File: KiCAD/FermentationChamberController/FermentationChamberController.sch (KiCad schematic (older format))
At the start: 18 parts, among them P1 Digital, P2 Analog

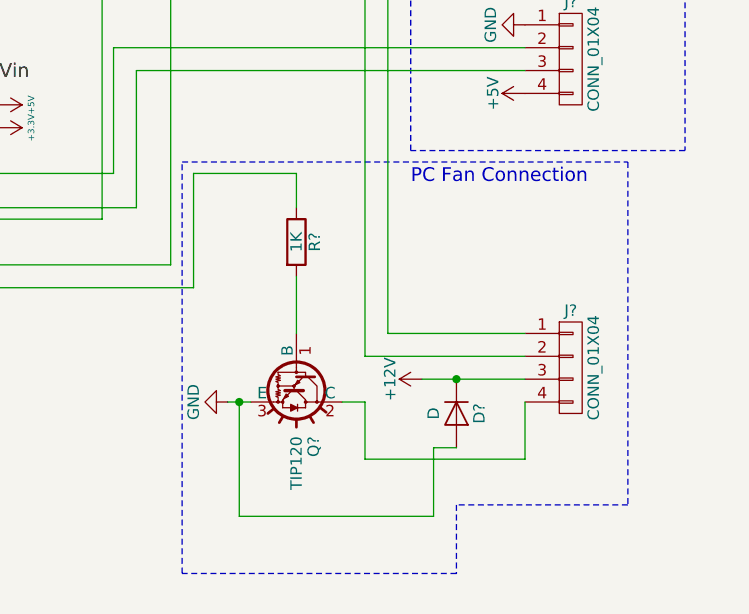
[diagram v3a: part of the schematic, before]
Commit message: And another correction to the diode
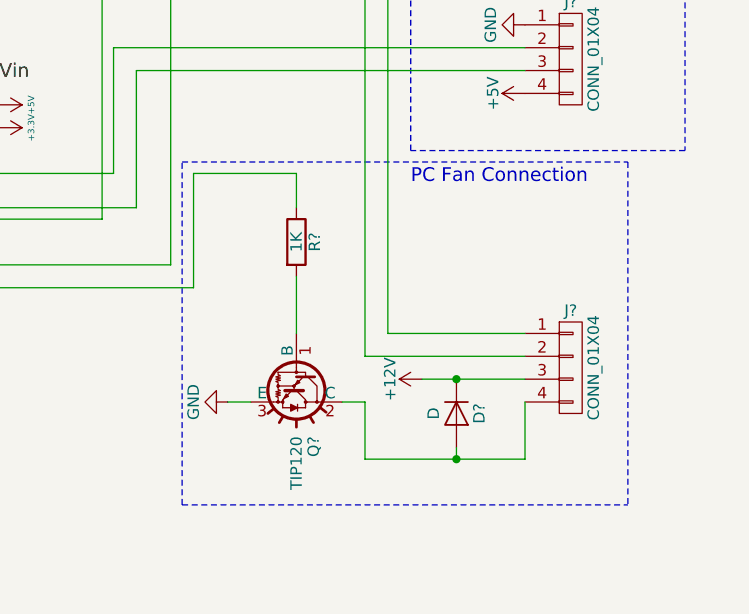
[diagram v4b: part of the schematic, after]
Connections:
- net GND: no longer D?.2 (A)
- net at J?.4 (P4), Q?.2 (C): now also D?.2 (A)
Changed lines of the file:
@@
 Wire Wire Line
 	5700 4900 5700 5050
-Connection ~ 5450 5900
 Wire Wire Line
 	5700 4900 5250 4900
@@
 	7400 3900 7400 4800
 Wire Notes Line
-	7150 6350 6400 6350
-Wire Notes Line
-	6400 6350 6400 6650
-Wire Notes Line
-	6400 6650 5200 6650
-Wire Notes Line
-	5200 6650 5200 4850
+	5200 6350 7150 6350
 Wire Notes Line
 	5200 4850 7150 4850
@@
 Connection ~ 6400 5800
 Wire Wire Line
-	5450 5900 5450 6400
-Wire Wire Line
-	5450 6400 6300 6400
-Wire Wire Line
-	6300 6400 6300 6100
-Wire Wire Line
-	6300 6100 6400 6100
-Wire Wire Line
 	6700 5900 6700 6150
 Wire Wire Line
@@
 Wire Wire Line
 	6000 6150 6000 5900
+Wire Wire Line
+	6400 6100 6400 6150
+Connection ~ 6400 6150
+Wire Notes Line
+	5200 6350 5200 4850
 $EndSCHEMATC

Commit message: Annotated
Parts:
- D1: renamed from D?; value D -> Diode
- gave numbers to parts that had none: 15
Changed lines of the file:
@@
 $EndComp
 $Comp
-L GND #PWR01
+L GND #PWR4
 U 1 1 56D7422C
 P 2750 3500
-F 0 "#PWR01" H 2750 3250 50  0001 C CNN
+F 0 "#PWR4" H 2750 3250 50  0001 C CNN
 F 1 "GND" H 2750 3350 50  0000 C CNN
 F 2 "" H 2750 3500 50  0000 C CNN
@@
 $EndComp
 $Comp
-L GND #PWR02
+L GND #PWR5
 U 1 1 56D746ED
 P 2750 4500
-F 0 "#PWR02" H 2750 4250 50  0001 C CNN
+F 0 "#PWR5" H 2750 4250 50  0001 C CNN
 F 1 "GND" H 2750 4350 50  0000 C CNN
 F 2 "" H 2750 4500 50  0000 C CNN
@@
 $EndComp
 $Comp
-L +5V #PWR03
+L +5V #PWR11
 U 1 1 56D747E8
 P 4400 4600
-F 0 "#PWR03" H 4400 4450 50  0001 C CNN
+F 0 "#PWR11" H 4400 4450 50  0001 C CNN
 F 1 "+5V" H 4400 4740 28  0000 C CNN
 F 2 "" H 4400 4600 50  0000 C CNN
@@
 $EndComp
 $Comp
-L +3.3V #PWR04
+L +3.3V #PWR12
 U 1 1 56D74854
 P 4400 4700
-F 0 "#PWR04" H 4400 4550 50  0001 C CNN
+F 0 "#PWR12" H 4400 4550 50  0001 C CNN
 F 1 "+3.3V" H 4400 4840 28  0000 C CNN
 F 2 "" H 4400 4700 50  0000 C CNN
@@
 1
 $Comp
-L LCD16X2 DS?
+L LCD16X2 DS1
 U 1 1 591B37D5
 P 3500 1150
-F 0 "DS?" H 2700 1550 50  0000 C CNN
+F 0 "DS1" H 2700 1550 50  0000 C CNN
 F 1 "LCD16X2" H 4200 1550 50  0000 C CNN
 F 2 "WC1602A" H 3500 1100 50  0001 C CIN
@@
 $EndComp
 $Comp
-L TIP120 Q?
+L TIP120 Q1
 U 1 1 591B3DDF
 P 5200 2150
-F 0 "Q?" H 5450 2225 50  0000 L CNN
+F 0 "Q1" H 5450 2225 50  0000 L CNN
 F 1 "TIP120" H 5450 2150 50  0000 L CNN
 F 2 "TO_SOT_Packages_THT:TO-220_Vertical" H 5450 2075 50  0001 L CIN
@@
 $EndComp
 $Comp
-L R R?
+L R R2
 U 1 1 591B3E76
 P 2950 2100
-F 0 "R?" V 3030 2100 50  0000 C CNN
+F 0 "R2" V 3030 2100 50  0000 C CNN
 F 1 "1.47K" V 2950 2100 50  0000 C CNN
 F 2 "" V 2880 2100 50  0001 C CNN
@@
 $EndComp
 $Comp
-L R R?
+L R R3
 U 1 1 591B3EE1
 P 4150 1850
-F 0 "R?" V 4230 1850 50  0000 C CNN
+F 0 "R3" V 4230 1850 50  0000 C CNN
 F 1 "220" V 4150 1850 50  0000 C CNN
 F 2 "" V 4080 1850 50  0001 C CNN
@@
 $EndComp
 $Comp
-L R R?
+L R R4
 U 1 1 591B3F3C
 P 4850 2350
-F 0 "R?" V 4930 2350 50  0000 C CNN
+F 0 "R4" V 4930 2350 50  0000 C CNN
 F 1 "2K" V 4850 2350 50  0000 C CNN
 F 2 "" V 4780 2350 50  0001 C CNN
@@
 	5300 1650 5300 1950
 $Comp
-L Earth #PWR?
+L Earth #PWR13
 U 1 1 591B481E
 P 5300 2400
-F 0 "#PWR?" H 5300 2150 50  0001 C CNN
+F 0 "#PWR13" H 5300 2150 50  0001 C CNN
 F 1 "Earth" H 5300 2250 50  0001 C CNN
 F 2 "" H 5300 2400 50  0001 C CNN
@@
 	5300 2400 5300 2350
 $Comp
-L Earth #PWR?
+L Earth #PWR3
 U 1 1 591B4871
 P 2750 1700
-F 0 "#PWR?" H 2750 1450 50  0001 C CNN
+F 0 "#PWR3" H 2750 1450 50  0001 C CNN
 F 1 "Earth" H 2750 1550 50  0001 C CNN
 F 2 "" H 2750 1700 50  0001 C CNN
@@
 	2750 1650 2750 1700
 $Comp
-L +5V #PWR?
+L +5V #PWR7
 U 1 1 591B4919
 P 2850 1700
-F 0 "#PWR?" H 2850 1550 50  0001 C CNN
+F 0 "#PWR7" H 2850 1550 50  0001 C CNN
 F 1 "+5V" H 2850 1840 50  0000 C CNN
 F 2 "" H 2850 1700 50  0001 C CNN
@@
 	2950 1650 2950 1950
 $Comp
-L Earth #PWR?
+L Earth #PWR8
 U 1 1 591B4B94
 P 2950 2250
-F 0 "#PWR?" H 2950 2000 50  0001 C CNN
+F 0 "#PWR8" H 2950 2000 50  0001 C CNN
 F 1 "Earth" H 2950 2100 50  0001 C CNN
 F 2 "" H 2950 2250 50  0001 C CNN
@@
 	4850 5100 2850 5100
 $Comp
-L Earth #PWR?
+L Earth #PWR9
 U 1 1 591B5084
 P 3150 1700
-F 0 "#PWR?" H 3150 1450 50  0001 C CNN
+F 0 "#PWR9" H 3150 1450 50  0001 C CNN
 F 1 "Earth" H 3150 1550 50  0001 C CNN
 F 2 "" H 3150 1700 50  0001 C CNN
@@
 	4150 1650 4150 1700
 $Comp
-L +5V #PWR?
+L +5V #PWR10
 U 1 1 591BA361
 P 4150 2000
-F 0 "#PWR?" H 4150 1850 50  0001 C CNN
+F 0 "#PWR10" H 4150 1850 50  0001 C CNN
 F 1 "+5V" H 4150 2140 50  0000 C CNN
 F 2 "" H 4150 2000 50  0001 C CNN
@@
 $EndComp
 $Comp
-L Rotary_Encoder_Switch SW?
+L Rotary_Encoder_Switch SW1
 U 1 1 591BA40F
 P 6100 1200
-F 0 "SW?" H 6100 1460 50  0000 C CNN
+F 0 "SW1" H 6100 1460 50  0000 C CNN
 F 1 "Rotary_Encoder_Switch" H 6100 940 50  0000 C CNN
 F 2 "" H 6000 1360 50  0001 C CNN
@@
 	6650 1300 6400 1300
 $Comp
-L +5V #PWR?
+L +5V #PWR17
 U 1 1 591BA55B
 P 6450 1100
-F 0 "#PWR?" H 6450 950 50  0001 C CNN
+F 0 "#PWR17" H 6450 950 50  0001 C CNN
 F 1 "+5V" H 6450 1240 50  0000 C CNN
 F 2 "" H 6450 1100 50  0001 C CNN
@@
 	6400 1100 6450 1100
 $Comp
-L R R?
+L R R6
 U 1 1 591BA5F0
 P 6800 1300
-F 0 "R?" V 6880 1300 50  0000 C CNN
+F 0 "R6" V 6880 1300 50  0000 C CNN
 F 1 "10K" V 6800 1300 50  0000 C CNN
 F 2 "" V 6730 1300 50  0001 C CNN
@@
 $EndComp
 $Comp
-L GND #PWR?
+L GND #PWR20
 U 1 1 591BA655
 P 7000 1300
-F 0 "#PWR?" H 7000 1050 50  0001 C CNN
+F 0 "#PWR20" H 7000 1050 50  0001 C CNN
 F 1 "GND" H 7000 1150 50  0000 C CNN
 F 2 "" H 7000 1300 50  0001 C CNN
@@
 	7000 1300 6950 1300
 $Comp
-L GND #PWR?
+L GND #PWR15
 U 1 1 591BA8F3
 P 5750 1200
-F 0 "#PWR?" H 5750 950 50  0001 C CNN
+F 0 "#PWR15" H 5750 950 50  0001 C CNN
 F 1 "GND" H 5750 1050 50  0000 C CNN
 F 2 "" H 5750 1200 50  0001 C CNN
@@
 	4650 1100 5800 1100
 $Comp
-L Screw_Terminal_1x02 J?
+L Screw_Terminal_1x02 J1
 U 1 1 591BAA85
 P 1000 6500
-F 0 "J?" H 1000 6750 50  0000 C TNN
+F 0 "J1" H 1000 6750 50  0000 C TNN
 F 1 "Screw_Terminal_1x02" V 850 6500 50  0000 C TNN
 F 2 "" H 1000 6275 50  0001 C CNN
@@
 $EndComp
 $Comp
-L Screw_Terminal_1x02 J?
+L Screw_Terminal_1x02 J2
 U 1 1 591BADC2
 P 1850 6500
-F 0 "J?" H 1850 6750 50  0000 C TNN
+F 0 "J2" H 1850 6750 50  0000 C TNN
 F 1 "Screw_Terminal_1x02" V 1700 6500 50  0000 C TNN
 F 2 "" H 1850 6275 50  0001 C CNN
@@
 $EndComp
 $Comp
-L Screw_Terminal_1x02 J?
+L Screw_Terminal_1x02 J3
 U 1 1 591BAE99
 P 2700 6500
-F 0 "J?" H 2700 6750 50  0000 C TNN
+F 0 "J3" H 2700 6750 50  0000 C TNN
 F 1 "Screw_Terminal_1x02" V 2550 6500 50  0000 C TNN
 F 2 "" H 2700 6275 50  0001 C CNN
@@
 Connection ~ 1750 5800
 $Comp
-L R R?
+L R R1
 U 1 1 591BB000
 P 1900 5550
-F 0 "R?" V 1980 5550 50  0000 C CNN
+F 0 "R1" V 1980 5550 50  0000 C CNN
 F 1 "4.7K" V 1800 5550 50  0000 C CNN
 F 2 "" V 1830 5550 50  0001 C CNN
@@
 $EndComp
 $Comp
-L +5V #PWR?
+L +5V #PWR2
 U 1 1 591BB0B3
 P 2150 5550
-F 0 "#PWR?" H 2150 5400 50  0001 C CNN
+F 0 "#PWR2" H 2150 5400 50  0001 C CNN
 F 1 "+5V" H 2150 5690 50  0000 C CNN
 F 2 "" H 2150 5550 50  0001 C CNN
@@
 Connection ~ 2150 5700
 $Comp
-L GND #PWR?
+L GND #PWR1
 U 1 1 591BB21C
 P 900 6200
-F 0 "#PWR?" H 900 5950 50  0001 C CNN
+F 0 "#PWR1" H 900 5950 50  0001 C CNN
 F 1 "GND" H 900 6050 50  0000 C CNN
 F 2 "" H 900 6200 50  0001 C CNN
@@
 $EndComp
 $Comp
-L GND #PWR?
+L GND #PWR6
 U 1 1 591BB255
 P 2800 6200
-F 0 "#PWR?" H 2800 5950 50  0001 C CNN
+F 0 "#PWR6" H 2800 5950 50  0001 C CNN
 F 1 "GND" H 2800 6050 50  0000 C CNN
 F 2 "" H 2800 6200 50  0001 C CNN
@@
 	3150 2800 3150 3600
 $Comp
-L CONN_01X04 J?
+L CONN_01X04 J5
 U 1 1 591BC121
 P 6900 5750
-F 0 "J?" H 6900 6000 50  0000 C CNN
+F 0 "J5" H 6900 6000 50  0000 C CNN
 F 1 "CONN_01X04" V 7000 5750 50  0000 C CNN
 F 2 "" H 6900 5750 50  0001 C CNN
@@
 $EndComp
 $Comp
-L TIP120 Q?
+L TIP120 Q2
 U 1 1 591BC33E
 P 5700 5800
-F 0 "Q?" H 5950 5875 50  0000 L CNN
+F 0 "Q2" H 5950 5875 50  0000 L CNN
 F 1 "TIP120" H 5950 5800 50  0000 L CNN
 F 2 "TO_SOT_Packages_THT:TO-220_Vertical" H 5950 5725 50  0001 L CIN
@@
 $EndComp
 $Comp
-L CONN_01X04 J?
+L CONN_01X04 J4
 U 1 1 591BC4F4
 P 6900 4400
-F 0 "J?" H 6900 4650 50  0000 C CNN
+F 0 "J4" H 6900 4650 50  0000 C CNN
 F 1 "CONN_01X04" V 7000 4400 50  0000 C CNN
 F 2 "" H 6900 4400 50  0001 C CNN
@@
 $EndComp
 $Comp
-L D D?
+L D D1
 U 1 1 591BC636
 P 6400 5950
-F 0 "D?" H 6400 6050 50  0000 C CNN
-F 1 "D" H 6400 5850 50  0000 C CNN
+F 0 "D1" H 6400 6050 50  0000 C CNN
+F 1 "Diode" H 6400 5850 50  0000 C CNN
 F 2 "" H 6400 5950 50  0001 C CNN
 F 3 "" H 6400 5950 50  0001 C CNN
@@
 $EndComp
 $Comp
-L R R?
+L R R5
 U 1 1 591BC750
 P 5700 5200
-F 0 "R?" V 5780 5200 50  0000 C CNN
+F 0 "R5" V 5780 5200 50  0000 C CNN
 F 1 "1K" V 5700 5200 50  0000 C CNN
 F 2 "" V 5630 5200 50  0001 C CNN
@@
 $EndComp
 $Comp
-L GND #PWR?
+L GND #PWR14
 U 1 1 591BCA6D
 P 5400 5900
-F 0 "#PWR?" H 5400 5650 50  0001 C CNN
+F 0 "#PWR14" H 5400 5650 50  0001 C CNN
 F 1 "GND" H 5400 5750 50  0000 C CNN
 F 2 "" H 5400 5900 50  0001 C CNN
@@
 	6100 2800 3850 2800
 $Comp
-L +5V #PWR?
+L +5V #PWR19
 U 1 1 591BDC18
 P 6700 4550
-F 0 "#PWR?" H 6700 4400 50  0001 C CNN
+F 0 "#PWR19" H 6700 4400 50  0001 C CNN
 F 1 "+5V" H 6700 4690 50  0000 C CNN
 F 2 "" H 6700 4550 50  0001 C CNN
@@
 	4900 4900 3350 4900
 $Comp
-L GND #PWR?
+L GND #PWR18
 U 1 1 591BE258
 P 6700 4250
-F 0 "#PWR?" H 6700 4000 50  0001 C CNN
+F 0 "#PWR18" H 6700 4000 50  0001 C CNN
 F 1 "GND" H 6700 4100 50  0000 C CNN
 F 2 "" H 6700 4250 50  0001 C CNN
@@
 Arduino Nano
 $Comp
-L +12V #PWR?
+L +12V #PWR16
 U 1 1 591BFE81
 P 6250 5800
-F 0 "#PWR?" H 6250 5650 50  0001 C CNN
+F 0 "#PWR16" H 6250 5650 50  0001 C CNN
 F 1 "+12V" H 6250 5940 50  0000 C CNN
 F 2 "" H 6250 5800 50  0001 C CNN

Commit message: Workign on the PCB Layout, first step.
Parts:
- D1: footprint (none) -> Diodes_THT:D_DO-15_P10.16mm_Horizontal
- DS1: footprint WC1602A -> Pin_Headers:Pin_Header_Straight_1x16_Pitch2.54mm
- J1, J2, J3: footprint (none) -> Connectors_Terminal_Blocks:TerminalBlock_WAGO-804_RM5mm_2pol
- J4, J5: footprint (none) -> Pin_Headers:Pin_Header_Straight_1x04_Pitch2.54mm
- P1, P2: footprint Socket_Arduino_Nano:Socket_Strip_Arduino_1x15 -> Pin_Headers:Pin_Header_Straight_1x15_Pitch2.54mm
- Q1: footprint TO_SOT_Packages_THT:TO-220_Vertical -> TO_SOT_Packages_THT:TO-220_Horizontal
- R1, R2, R3, R4, R5, R6: footprint (none) -> Resistors_THT:R_Axial_DIN0207_L6.3mm_D2.5mm_P10.16mm_Horizontal
- SW1: footprint (none) -> Pin_Headers:Pin_Header_Straight_1x05_Pitch2.54mm
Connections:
- net 10(**/SS): now also R1.1
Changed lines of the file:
@@
 F 0 "P1" H 3550 4600 50  0000 C CNN
 F 1 "Digital" V 3650 3800 50  0000 C CNN
-F 2 "Socket_Arduino_Nano:Socket_Strip_Arduino_1x15" H 3550 3800 50  0001 C CNN
+F 2 "Pin_Headers:Pin_Header_Straight_1x15_Pitch2.54mm" H 3550 3800 50  0001 C CNN
 F 3 "" H 3550 3800 50  0000 C CNN
 	1    3550 3800
@@
 F 0 "P2" H 3550 5000 50  0000 C CNN
 F 1 "Analog" V 3650 4200 50  0000 C CNN
-F 2 "Socket_Arduino_Nano:Socket_Strip_Arduino_1x15" H 3550 4200 50  0001 C CNN
+F 2 "Pin_Headers:Pin_Header_Straight_1x15_Pitch2.54mm" H 3550 4200 50  0001 C CNN
 F 3 "" H 3550 4200 50  0000 C CNN
 	1    3550 4200
@@
 $EndComp
 $Comp
-L GND #PWR4
+L GND #PWR01
 U 1 1 56D7422C
 P 2750 3500
-F 0 "#PWR4" H 2750 3250 50  0001 C CNN
+F 0 "#PWR01" H 2750 3250 50  0001 C CNN
 F 1 "GND" H 2750 3350 50  0000 C CNN
 F 2 "" H 2750 3500 50  0000 C CNN
@@
 $EndComp
 $Comp
-L GND #PWR5
+L GND #PWR02
 U 1 1 56D746ED
 P 2750 4500
-F 0 "#PWR5" H 2750 4250 50  0001 C CNN
+F 0 "#PWR02" H 2750 4250 50  0001 C CNN
 F 1 "GND" H 2750 4350 50  0000 C CNN
 F 2 "" H 2750 4500 50  0000 C CNN
@@
 $EndComp
 $Comp
-L +5V #PWR11
+L +5V #PWR03
 U 1 1 56D747E8
 P 4400 4600
-F 0 "#PWR11" H 4400 4450 50  0001 C CNN
+F 0 "#PWR03" H 4400 4450 50  0001 C CNN
 F 1 "+5V" H 4400 4740 28  0000 C CNN
 F 2 "" H 4400 4600 50  0000 C CNN
@@
 $EndComp
 $Comp
-L +3.3V #PWR12
+L +3.3V #PWR04
 U 1 1 56D74854
 P 4400 4700
-F 0 "#PWR12" H 4400 4550 50  0001 C CNN
+F 0 "#PWR04" H 4400 4550 50  0001 C CNN
 F 1 "+3.3V" H 4400 4840 28  0000 C CNN
 F 2 "" H 4400 4700 50  0000 C CNN
@@
 F 0 "DS1" H 2700 1550 50  0000 C CNN
 F 1 "LCD16X2" H 4200 1550 50  0000 C CNN
-F 2 "WC1602A" H 3500 1100 50  0001 C CIN
+F 2 "Pin_Headers:Pin_Header_Straight_1x16_Pitch2.54mm" H 3500 1100 50  0001 C CIN
 F 3 "" H 3500 1150 50  0001 C CNN
 	1    3500 1150
@@
 F 0 "Q1" H 5450 2225 50  0000 L CNN
 F 1 "TIP120" H 5450 2150 50  0000 L CNN
-F 2 "TO_SOT_Packages_THT:TO-220_Vertical" H 5450 2075 50  0001 L CIN
+F 2 "TO_SOT_Packages_THT:TO-220_Horizontal" H 5450 2075 50  0001 L CIN
 F 3 "" H 5200 2150 50  0001 L CNN
 	1    5200 2150
@@
 F 0 "R2" V 3030 2100 50  0000 C CNN
 F 1 "1.47K" V 2950 2100 50  0000 C CNN
-F 2 "" V 2880 2100 50  0001 C CNN
+F 2 "Resistors_THT:R_Axial_DIN0207_L6.3mm_D2.5mm_P10.16mm_Horizontal" V 2880 2100 50  0001 C CNN
 F 3 "" H 2950 2100 50  0001 C CNN
 	1    2950 2100
@@
 F 0 "R3" V 4230 1850 50  0000 C CNN
 F 1 "220" V 4150 1850 50  0000 C CNN
-F 2 "" V 4080 1850 50  0001 C CNN
+F 2 "Resistors_THT:R_Axial_DIN0207_L6.3mm_D2.5mm_P10.16mm_Horizontal" V 4080 1850 50  0001 C CNN
 F 3 "" H 4150 1850 50  0001 C CNN
 	1    4150 1850
@@
 F 0 "R4" V 4930 2350 50  0000 C CNN
 F 1 "2K" V 4850 2350 50  0000 C CNN
-F 2 "" V 4780 2350 50  0001 C CNN
+F 2 "Resistors_THT:R_Axial_DIN0207_L6.3mm_D2.5mm_P10.16mm_Horizontal" V 4780 2350 50  0001 C CNN
 F 3 "" H 4850 2350 50  0001 C CNN
 	1    4850 2350
@@
 	5300 1650 5300 1950
 $Comp
-L Earth #PWR13
+L Earth #PWR05
 U 1 1 591B481E
 P 5300 2400
-F 0 "#PWR13" H 5300 2150 50  0001 C CNN
+F 0 "#PWR05" H 5300 2150 50  0001 C CNN
 F 1 "Earth" H 5300 2250 50  0001 C CNN
 F 2 "" H 5300 2400 50  0001 C CNN
@@
 	5300 2400 5300 2350
 $Comp
-L Earth #PWR3
+L Earth #PWR06
 U 1 1 591B4871
 P 2750 1700
-F 0 "#PWR3" H 2750 1450 50  0001 C CNN
+F 0 "#PWR06" H 2750 1450 50  0001 C CNN
 F 1 "Earth" H 2750 1550 50  0001 C CNN
 F 2 "" H 2750 1700 50  0001 C CNN
@@
 	2750 1650 2750 1700
 $Comp
-L +5V #PWR7
+L +5V #PWR07
 U 1 1 591B4919
 P 2850 1700
-F 0 "#PWR7" H 2850 1550 50  0001 C CNN
+F 0 "#PWR07" H 2850 1550 50  0001 C CNN
 F 1 "+5V" H 2850 1840 50  0000 C CNN
 F 2 "" H 2850 1700 50  0001 C CNN
@@
 	2950 1650 2950 1950
 $Comp
-L Earth #PWR8
+L Earth #PWR08
 U 1 1 591B4B94
 P 2950 2250
-F 0 "#PWR8" H 2950 2000 50  0001 C CNN
+F 0 "#PWR08" H 2950 2000 50  0001 C CNN
 F 1 "Earth" H 2950 2100 50  0001 C CNN
 F 2 "" H 2950 2250 50  0001 C CNN
@@
 	4850 5100 2850 5100
 $Comp
-L Earth #PWR9
+L Earth #PWR09
 U 1 1 591B5084
 P 3150 1700
-F 0 "#PWR9" H 3150 1450 50  0001 C CNN
+F 0 "#PWR09" H 3150 1450 50  0001 C CNN
 F 1 "Earth" H 3150 1550 50  0001 C CNN
 F 2 "" H 3150 1700 50  0001 C CNN
@@
 	4150 1650 4150 1700
 $Comp
-L +5V #PWR10
+L +5V #PWR010
 U 1 1 591BA361
 P 4150 2000
-F 0 "#PWR10" H 4150 1850 50  0001 C CNN
+F 0 "#PWR010" H 4150 1850 50  0001 C CNN
 F 1 "+5V" H 4150 2140 50  0000 C CNN
 F 2 "" H 4150 2000 50  0001 C CNN
@@
 F 0 "SW1" H 6100 1460 50  0000 C CNN
 F 1 "Rotary_Encoder_Switch" H 6100 940 50  0000 C CNN
-F 2 "" H 6000 1360 50  0001 C CNN
+F 2 "Pin_Headers:Pin_Header_Straight_1x05_Pitch2.54mm" H 6000 1360 50  0001 C CNN
 F 3 "" H 6100 1460 50  0001 C CNN
 	1    6100 1200
@@
 	6650 1300 6400 1300
 $Comp
-L +5V #PWR17
+L +5V #PWR011
 U 1 1 591BA55B
 P 6450 1100
-F 0 "#PWR17" H 6450 950 50  0001 C CNN
+F 0 "#PWR011" H 6450 950 50  0001 C CNN
 F 1 "+5V" H 6450 1240 50  0000 C CNN
 F 2 "" H 6450 1100 50  0001 C CNN
@@
 F 0 "R6" V 6880 1300 50  0000 C CNN
 F 1 "10K" V 6800 1300 50  0000 C CNN
-F 2 "" V 6730 1300 50  0001 C CNN
+F 2 "Resistors_THT:R_Axial_DIN0207_L6.3mm_D2.5mm_P10.16mm_Horizontal" V 6730 1300 50  0001 C CNN
 F 3 "" H 6800 1300 50  0001 C CNN
 	1    6800 1300
@@
 $EndComp
 $Comp
-L GND #PWR20
+L GND #PWR012
 U 1 1 591BA655
 P 7000 1300
-F 0 "#PWR20" H 7000 1050 50  0001 C CNN
+F 0 "#PWR012" H 7000 1050 50  0001 C CNN
 F 1 "GND" H 7000 1150 50  0000 C CNN
 F 2 "" H 7000 1300 50  0001 C CNN
@@
 	7000 1300 6950 1300
 $Comp
-L GND #PWR15
+L GND #PWR013
 U 1 1 591BA8F3
 P 5750 1200
-F 0 "#PWR15" H 5750 950 50  0001 C CNN
+F 0 "#PWR013" H 5750 950 50  0001 C CNN
 F 1 "GND" H 5750 1050 50  0000 C CNN
 F 2 "" H 5750 1200 50  0001 C CNN
@@
 F 0 "J1" H 1000 6750 50  0000 C TNN
 F 1 "Screw_Terminal_1x02" V 850 6500 50  0000 C TNN
-F 2 "" H 1000 6275 50  0001 C CNN
+F 2 "Connectors_Terminal_Blocks:TerminalBlock_WAGO-804_RM5mm_2pol" H 1000 6275 50  0001 C CNN
 F 3 "" H 975 6500 50  0001 C CNN
 	1    1000 6500
@@
 F 0 "J2" H 1850 6750 50  0000 C TNN
 F 1 "Screw_Terminal_1x02" V 1700 6500 50  0000 C TNN
-F 2 "" H 1850 6275 50  0001 C CNN
+F 2 "Connectors_Terminal_Blocks:TerminalBlock_WAGO-804_RM5mm_2pol" H 1850 6275 50  0001 C CNN
 F 3 "" H 1825 6500 50  0001 C CNN
 	1    1850 6500
@@
 F 0 "J3" H 2700 6750 50  0000 C TNN
 F 1 "Screw_Terminal_1x02" V 2550 6500 50  0000 C TNN
-F 2 "" H 2700 6275 50  0001 C CNN
+F 2 "Connectors_Terminal_Blocks:TerminalBlock_WAGO-804_RM5mm_2pol" H 2700 6275 50  0001 C CNN
 F 3 "" H 2675 6500 50  0001 C CNN
 	1    2700 6500
@@
 F 0 "R1" V 1980 5550 50  0000 C CNN
 F 1 "4.7K" V 1800 5550 50  0000 C CNN
-F 2 "" V 1830 5550 50  0001 C CNN
+F 2 "Resistors_THT:R_Axial_DIN0207_L6.3mm_D2.5mm_P10.16mm_Horizontal" V 1830 5550 50  0001 C CNN
 F 3 "" H 1900 5550 50  0001 C CNN
 	1    1900 5550
@@
 $EndComp
 $Comp
-L +5V #PWR2
+L +5V #PWR014
 U 1 1 591BB0B3
 P 2150 5550
-F 0 "#PWR2" H 2150 5400 50  0001 C CNN
+F 0 "#PWR014" H 2150 5400 50  0001 C CNN
 F 1 "+5V" H 2150 5690 50  0000 C CNN
 F 2 "" H 2150 5550 50  0001 C CNN
@@
 Connection ~ 2150 5700
 $Comp
-L GND #PWR1
+L GND #PWR015
 U 1 1 591BB21C
 P 900 6200
-F 0 "#PWR1" H 900 5950 50  0001 C CNN
+F 0 "#PWR015" H 900 5950 50  0001 C CNN
 F 1 "GND" H 900 6050 50  0000 C CNN
 F 2 "" H 900 6200 50  0001 C CNN
@@
 $EndComp
 $Comp
-L GND #PWR6
+L GND #PWR016
 U 1 1 591BB255
 P 2800 6200
-F 0 "#PWR6" H 2800 5950 50  0001 C CNN
+F 0 "#PWR016" H 2800 5950 50  0001 C CNN
 F 1 "GND" H 2800 6050 50  0000 C CNN
 F 2 "" H 2800 6200 50  0001 C CNN
@@
 F 0 "J5" H 6900 6000 50  0000 C CNN
 F 1 "CONN_01X04" V 7000 5750 50  0000 C CNN
-F 2 "" H 6900 5750 50  0001 C CNN
+F 2 "Pin_Headers:Pin_Header_Straight_1x04_Pitch2.54mm" H 6900 5750 50  0001 C CNN
 F 3 "" H 6900 5750 50  0001 C CNN
 	1    6900 5750
@@
 F 0 "J4" H 6900 4650 50  0000 C CNN
 F 1 "CONN_01X04" V 7000 4400 50  0000 C CNN
-F 2 "" H 6900 4400 50  0001 C CNN
+F 2 "Pin_Headers:Pin_Header_Straight_1x04_Pitch2.54mm" H 6900 4400 50  0001 C CNN
 F 3 "" H 6900 4400 50  0001 C CNN
 	1    6900 4400
@@
 F 0 "D1" H 6400 6050 50  0000 C CNN
 F 1 "Diode" H 6400 5850 50  0000 C CNN
-F 2 "" H 6400 5950 50  0001 C CNN
+F 2 "Diodes_THT:D_DO-15_P10.16mm_Horizontal" H 6400 5950 50  0001 C CNN
 F 3 "" H 6400 5950 50  0001 C CNN
 	1    6400 5950
@@
 F 0 "R5" V 5780 5200 50  0000 C CNN
 F 1 "1K" V 5700 5200 50  0000 C CNN
-F 2 "" V 5630 5200 50  0001 C CNN
+F 2 "Resistors_THT:R_Axial_DIN0207_L6.3mm_D2.5mm_P10.16mm_Horizontal" V 5630 5200 50  0001 C CNN
 F 3 "" H 5700 5200 50  0001 C CNN
 	1    5700 5200
@@
 $EndComp
 $Comp
-L GND #PWR14
+L GND #PWR017
 U 1 1 591BCA6D
 P 5400 5900
-F 0 "#PWR14" H 5400 5650 50  0001 C CNN
+F 0 "#PWR017" H 5400 5650 50  0001 C CNN
 F 1 "GND" H 5400 5750 50  0000 C CNN
 F 2 "" H 5400 5900 50  0001 C CNN
@@
 	6100 2800 3850 2800
 $Comp
-L +5V #PWR19
+L +5V #PWR018
 U 1 1 591BDC18
 P 6700 4550
-F 0 "#PWR19" H 6700 4400 50  0001 C CNN
+F 0 "#PWR018" H 6700 4400 50  0001 C CNN
 F 1 "+5V" H 6700 4690 50  0000 C CNN
 F 2 "" H 6700 4550 50  0001 C CNN
@@
 	4900 4900 3350 4900
 $Comp
-L GND #PWR18
+L GND #PWR019
 U 1 1 591BE258
 P 6700 4250
-F 0 "#PWR18" H 6700 4000 50  0001 C CNN
+F 0 "#PWR019" H 6700 4000 50  0001 C CNN
 F 1 "GND" H 6700 4100 50  0000 C CNN
 F 2 "" H 6700 4250 50  0001 C CNN
@@
 Arduino Nano
 $Comp
-L +12V #PWR16
+L +12V #PWR020
 U 1 1 591BFE81
 P 6250 5800
-F 0 "#PWR16" H 6250 5650 50  0001 C CNN
+F 0 "#PWR020" H 6250 5650 50  0001 C CNN
 F 1 "+12V" H 6250 5940 50  0000 C CNN
 F 2 "" H 6250 5800 50  0001 C CNN
@@
 Wire Notes Line
 	5200 6350 5200 4850
+Connection ~ 1750 5550
+Connection ~ 6650 1300
 $EndSCHEMATC
